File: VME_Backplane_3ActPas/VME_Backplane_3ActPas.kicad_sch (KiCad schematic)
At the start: 0 parts

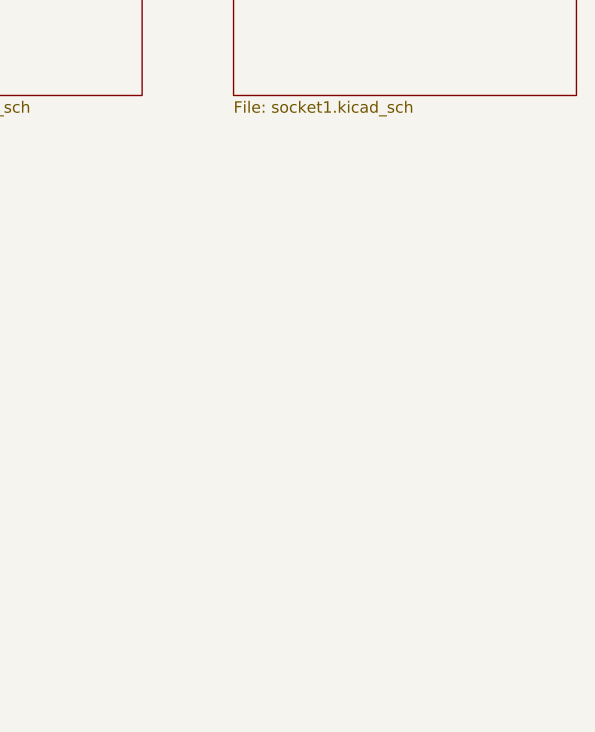
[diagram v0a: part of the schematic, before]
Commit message: Expand schematics to 3 slots
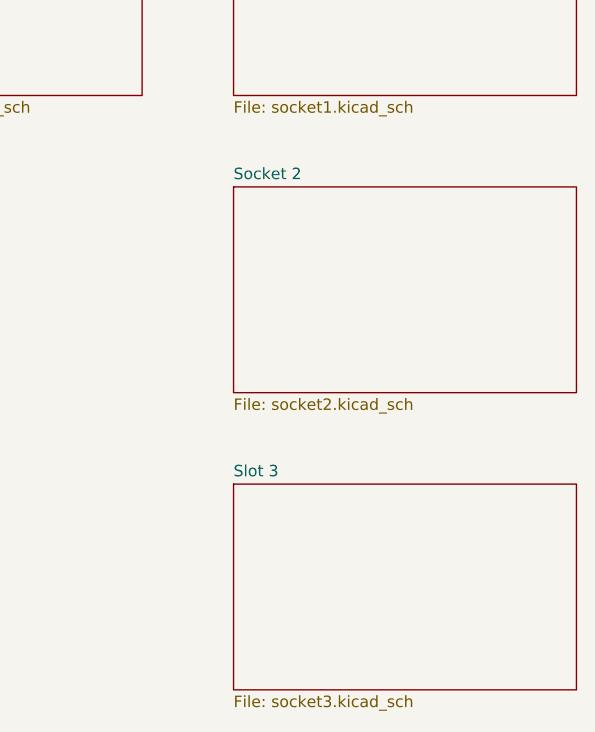
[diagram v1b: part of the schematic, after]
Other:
- added sheet Slot 3 (socket3.kicad_sch)
- added sheet Socket 2 (socket2.kicad_sch)

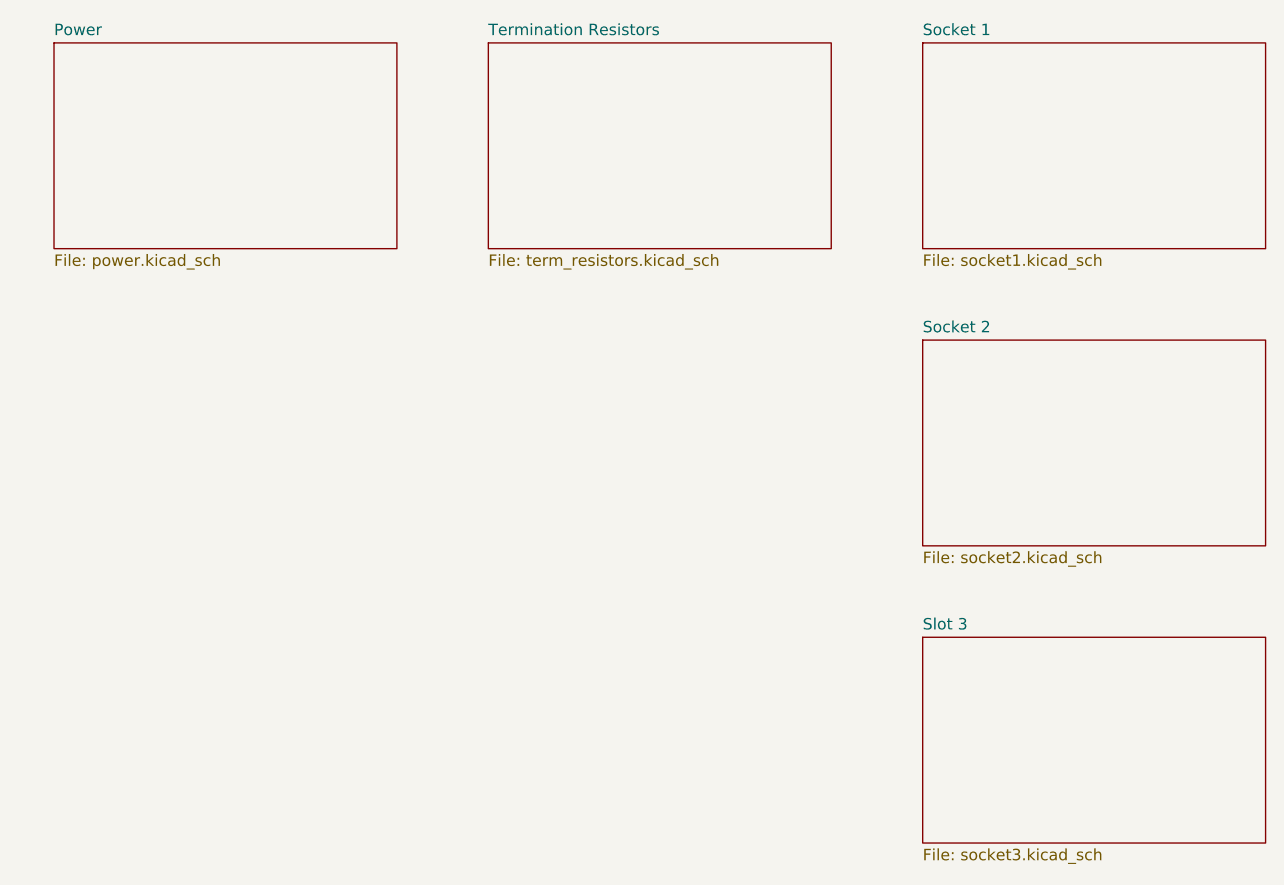
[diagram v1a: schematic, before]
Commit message: Layout work so far, mostly bus signals
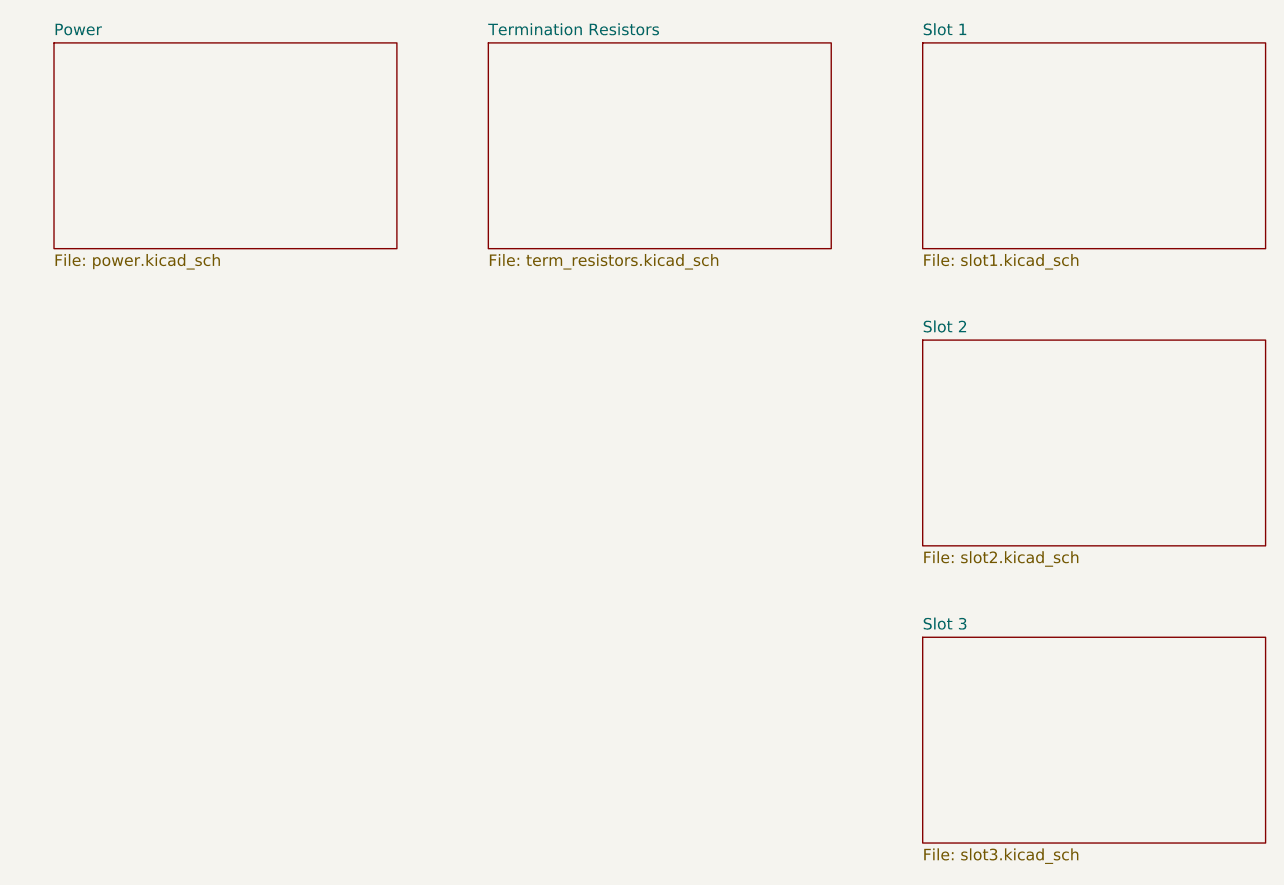
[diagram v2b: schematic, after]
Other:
- sheet Socket 1 renamed Slot 1
- sheet Socket 2 renamed Slot 2
- sheet Slot 1: file socket1.kicad_sch -> slot1.kicad_sch
- sheet Slot 2: file socket2.kicad_sch -> slot2.kicad_sch
- sheet Slot 3: file socket3.kicad_sch -> slot3.kicad_sch
- title: (none) -> 3 SLOT ACTIVE/PASSIVE TERMINATION VMEBUS BACKPLANE

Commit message: Add/update revision information in schematics and PCB
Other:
- company: (C) TOM STOREY -> TOM STOREY
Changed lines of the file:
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@@
   (title_block
     (title "3 SLOT ACTIVE/PASSIVE TERMINATION VMEBUS BACKPLANE")
-    (date "2024-01-02")
+    (date "2024-01-03")
     (rev "1")
-    (company "(C) TOM STOREY")
+    (company "TOM STOREY")
     (comment 1 "FREE FOR NON-COMMERCIAL USE")
   )

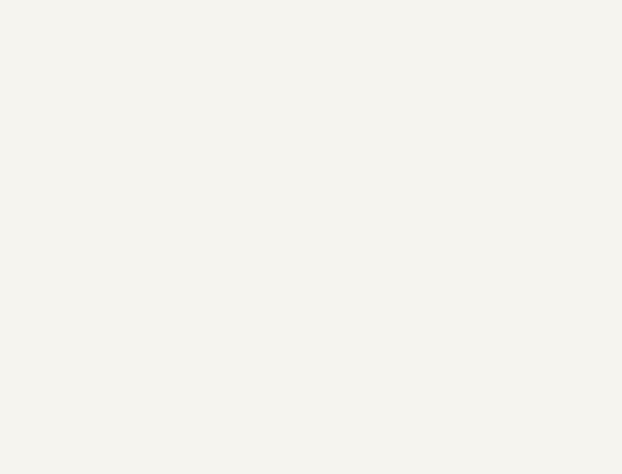
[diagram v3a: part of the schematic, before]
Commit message: Add X1 header, update release dates
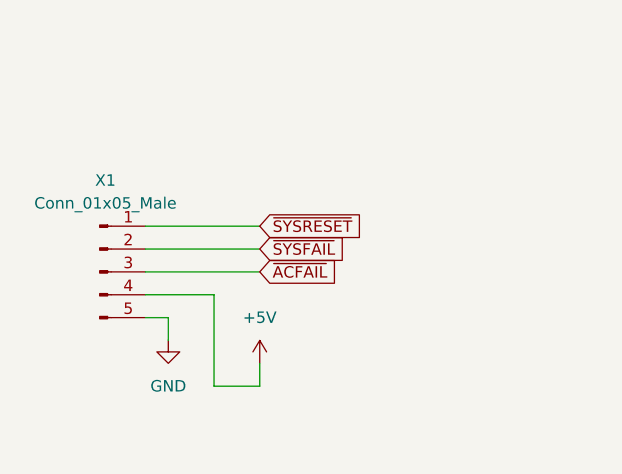
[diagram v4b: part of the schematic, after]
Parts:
- added X1: Conn_01x05_Male, Connector_PinHeader_2.54mm:PinHeader_1x05_P2.54mm_Vertical, symbol Connector:Conn_01x05_Male
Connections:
- new net +5V: X1.4 (Pin_4)
- new net GND: X1.5 (Pin_5)
- new net ~{ACFAIL}: X1.3 (Pin_3)
- new net ~{SYSFAIL}: X1.2 (Pin_2)
- new net ~{SYSRESET}: X1.1 (Pin_1)
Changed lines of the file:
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@@
   (title_block
     (title "3 SLOT ACTIVE/PASSIVE TERMINATION VMEBUS BACKPLANE")
-    (date "2024-01-03")
+    (date "2024-01-04")
     (rev "1")
     (company "TOM STOREY")
     (comment 1 "FREE FOR NON-COMMERCIAL USE")
+  )
+  (wire (pts (xy 50.8 106.68) (xy 53.34 106.68))
+    (stroke (width 0) (type default) (color 0 0 0 0))
+  )
+  (wire (pts (xy 58.42 104.14) (xy 58.42 114.3))
+    (stroke (width 0) (type default) (color 0 0 0 0))
+  )
+  (wire (pts (xy 50.8 101.6) (xy 63.5 101.6))
+    (stroke (width 0) (type default) (color 0 0 0 0))
+  )
+  (wire (pts (xy 50.8 104.14) (xy 58.42 104.14))
+    (stroke (width 0) (type default) (color 0 0 0 0))
+  )
+  (wire (pts (xy 63.5 111.76) (xy 63.5 114.3))
+    (stroke (width 0) (type default) (color 0 0 0 0))
+  )
+  (wire (pts (xy 53.34 106.68) (xy 53.34 109.22))
+    (stroke (width 0) (type default) (color 0 0 0 0))
+  )
+  (wire (pts (xy 50.8 99.06) (xy 63.5 99.06))
+    (stroke (width 0) (type default) (color 0 0 0 0))
+  )
+  (wire (pts (xy 58.42 114.3) (xy 63.5 114.3))
+    (stroke (width 0) (type default) (color 0 0 0 0))
+  )
+  (wire (pts (xy 50.8 96.52) (xy 63.5 96.52))
+    (stroke (width 0) (type default) (color 0 0 0 0))
+  )
+  (global_label "~{ACFAIL}" (shape input) (at 63.5 101.6 0) (fields_autoplaced)
+    (effects (font (size 1.27 1.27)) (justify left))
+    (property "Intersheet References" "${INTERSHEET_REFS}" (id 0) (at 72.0817 101.5206 0)
+      (effects (font (size 1.27 1.27)) (justify left) hide)
+    )
+  )
+  (global_label "~{SYSRESET}" (shape input) (at 63.5 96.52 0) (fields_autoplaced)
+    (effects (font (size 1.27 1.27)) (justify left))
+    (property "Intersheet References" "${INTERSHEET_REFS}" (id 0) (at 75.166 96.4406 0)
+      (effects (font (size 1.27 1.27)) (justify left) hide)
+    )
+  )
+  (global_label "~{SYSFAIL}" (shape input) (at 63.5 99.06 0) (fields_autoplaced)
+    (effects (font (size 1.27 1.27)) (justify left))
+    (property "Intersheet References" "${INTERSHEET_REFS}" (id 0) (at 73.2307 98.9806 0)
+      (effects (font (size 1.27 1.27)) (justify left) hide)
+    )
+  )
+  (symbol (lib_id "power:+5V") (at 63.5 111.76 0) (unit 1)
+    (in_bom yes) (on_board yes) (fields_autoplaced)
+    (property "Reference" "#PWR0136" (id 0) (at 63.5 115.57 0)
+      (effects (font (size 1.27 1.27)) hide)
+    )
+    (property "Value" "+5V" (id 1) (at 63.5 106.68 0))
+    (property "Footprint" "" (id 2) (at 63.5 111.76 0)
+      (effects (font (size 1.27 1.27)) hide)
+    )
+    (property "Datasheet" "" (id 3) (at 63.5 111.76 0)
+      (effects (font (size 1.27 1.27)) hide)
+    )
+    (pin "1")
+  )
+  (symbol (lib_id "Connector:Conn_01x05_Male") (at 45.72 101.6 0) (unit 1)
+    (in_bom yes) (on_board yes) (fields_autoplaced)
+    (property "Reference" "X1" (id 0) (at 46.355 91.44 0))
+    (property "Value" "Conn_01x05_Male" (id 1) (at 46.355 93.98 0))
+    (property "Footprint" "Connector_PinHeader_2.54mm:PinHeader_1x05_P2.54mm_Vertical" (id 2) (at 45.72 101.6 0)
+      (effects (font (size 1.27 1.27)) hide)
+    )
+    (property "Datasheet" "~" (id 3) (at 45.72 101.6 0)
+      (effects (font (size 1.27 1.27)) hide)
+    )
+    (pin "1")
+    (pin "2")
+    (pin "3")
+    (pin "4")
+    (pin "5")
+  )
+  (symbol (lib_id "power:GND") (at 53.34 109.22 0) (unit 1)
+    (in_bom yes) (on_board yes) (fields_autoplaced)
+    (property "Reference" "#PWR0137" (id 0) (at 53.34 115.57 0)
+      (effects (font (size 1.27 1.27)) hide)
+    )
+    (property "Value" "GND" (id 1) (at 53.34 114.3 0))
+    (property "Footprint" "" (id 2) (at 53.34 109.22 0)
+      (effects (font (size 1.27 1.27)) hide)
+    )
+    (property "Datasheet" "" (id 3) (at 53.34 109.22 0)
+      (effects (font (size 1.27 1.27)) hide)
+    )
+    (pin "1")
   )
   (sheet (at 40.64 30.48) (size 38.1 22.86) (fields_autoplaced)
@@
       (reference "#PWR0135") (unit 1) (value "+BATT") (footprint "")
     )
+    (path "/67b96dcb-cea3-4204-b786-8bb40fdae53f"
+      (reference "#PWR0136") (unit 1) (value "+5V") (footprint "")
+    )
+    (path "/da1098e2-634f-4ac8-86d6-224baa8f81ee"
+      (reference "#PWR0137") (unit 1) (value "GND") (footprint "")
+    )
     (path "/a0862581-9ad8-4f93-908d-f8764efb062e/69fbe2ce-7b1e-437f-852e-0c1529c0fc75"
       (reference "C1") (unit 1) (value "100nF") (footprint "Capacitor_THT:C_Disc_D4.3mm_W1.9mm_P5.00mm")
@@
       (reference "V5") (unit 1) (value "1N4148") (footprint "Diode_THT:D_DO-35_SOD27_P10.16mm_Horizontal")
     )
-    (path "/246231bb-ffb7-4bc4-ae1f-2359f6ae3062/be48314f-6816-4de8-9c2a-9aafb904566a"
-      (reference "X1") (unit 1) (value "Conn_01x05") (footprint "TerminalBlock_Phoenix:TerminalBlock_Phoenix_MKDS-1,5-5-5.08_1x05_P5.08mm_Horizontal")
+    (path "/bbcbcf1e-4451-4bd9-b215-8c189d13496c"
+      (reference "X1") (unit 1) (value "Conn_01x05_Male") (footprint "Connector_PinHeader_2.54mm:PinHeader_1x05_P2.54mm_Vertical")
     )
     (path "/a0862581-9ad8-4f93-908d-f8764efb062e/e0924cbb-7102-4d43-acb7-a2388aa3a950"
@@
       (reference "X3L1") (unit 1) (value "LO_R") (footprint "Connector_PinHeader_2.54mm:PinHeader_1x03_P2.54mm_Vertical")
     )
+    (path "/246231bb-ffb7-4bc4-ae1f-2359f6ae3062/be48314f-6816-4de8-9c2a-9aafb904566a"
+      (reference "X50") (unit 1) (value "Conn_01x05") (footprint "TerminalBlock_Phoenix:TerminalBlock_Phoenix_MKDS-1,5-5-5.08_1x05_P5.08mm_Horizontal")
+    )
     (path "/d65a77fd-c4df-4617-a5a6-70a784b7b841/976f9a9b-6fb6-4ca6-a9bf-e6c2cf1db92b"
